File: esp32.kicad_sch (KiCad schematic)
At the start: 17 parts, among them Q3 BSS670S2, U2 ESP32-S3-WROOM-1U

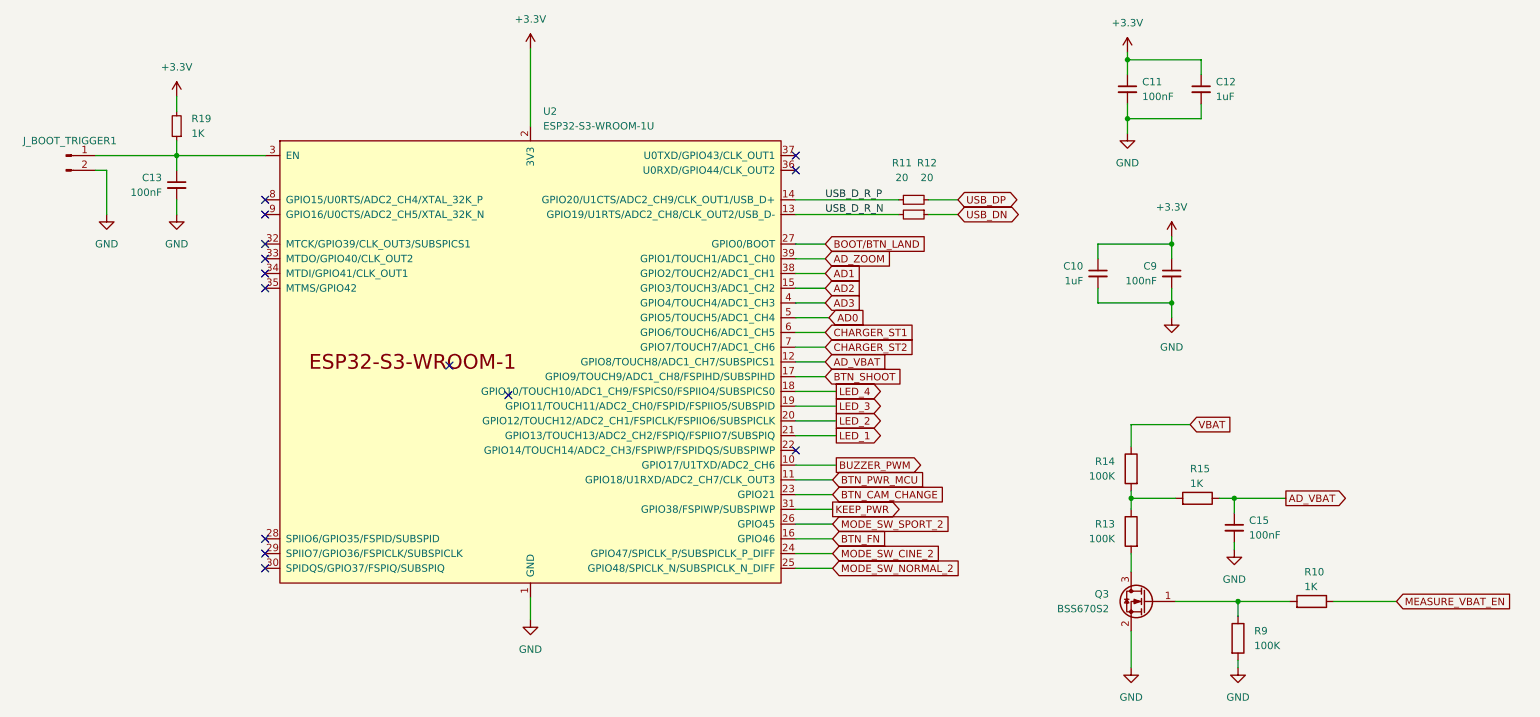
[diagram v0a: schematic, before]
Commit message: Board had been routedy
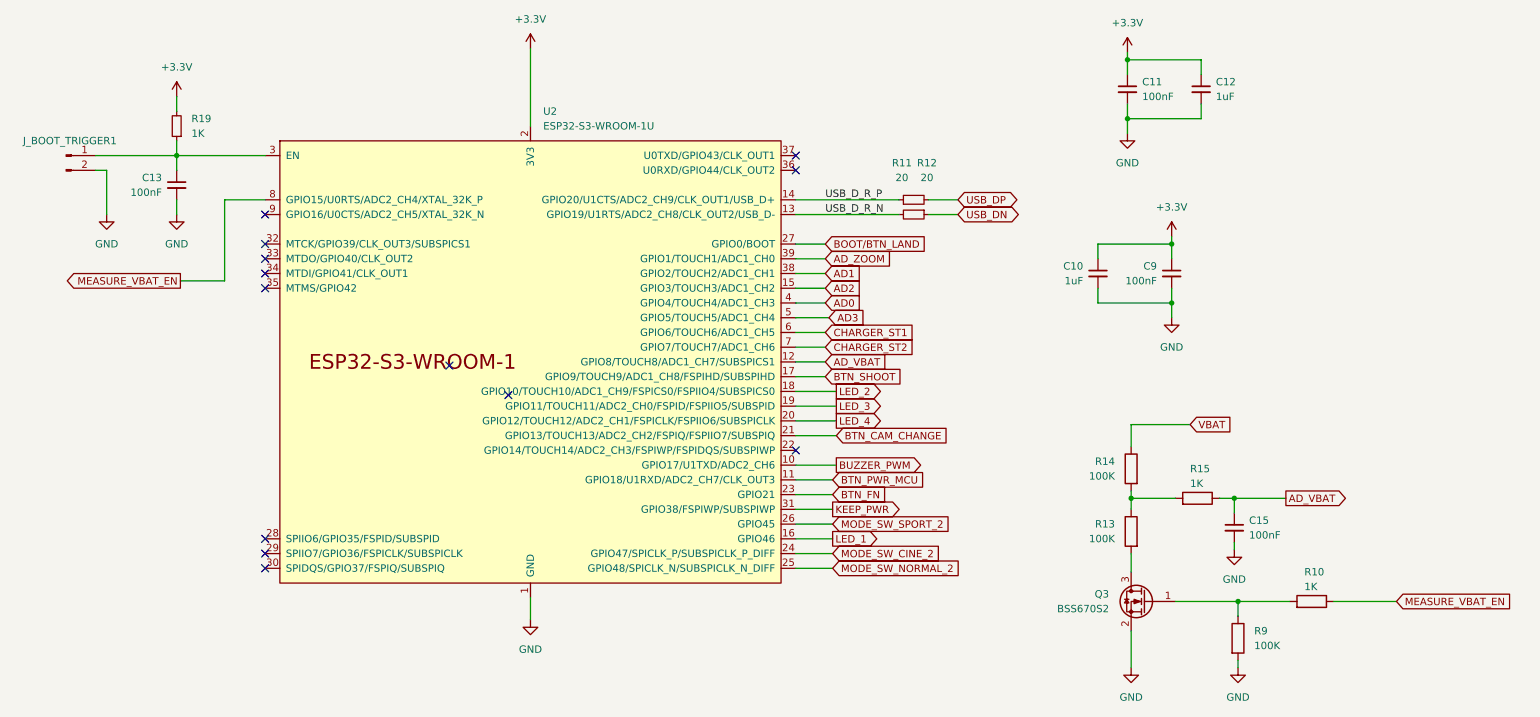
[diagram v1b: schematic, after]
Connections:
- net AD0: now also U2.4 (GPIO4/TOUCH4/ADC1_CH3); no longer U2.5 (GPIO5/TOUCH5/ADC1_CH4)
- net AD3: now also U2.5 (GPIO5/TOUCH5/ADC1_CH4); no longer U2.4 (GPIO4/TOUCH4/ADC1_CH3)
- net BTN_CAM_CHANGE: now also U2.21 (GPIO13/TOUCH13/ADC2_CH2/FSPIQ/FSPIIO7/SUBSPIQ); no longer U2.23 (GPIO21)
- net BTN_FN: now also U2.23 (GPIO21); no longer U2.16 (GPIO46)
- net LED_1: now also U2.16 (GPIO46); no longer U2.21 (GPIO13/TOUCH13/ADC2_CH2/FSPIQ/FSPIIO7/SUBSPIQ)
- net LED_2: now also U2.18 (GPIO10/TOUCH10/ADC1_CH9/FSPICS0/FSPIIO4/SUBSPICS0); no longer U2.20 (GPIO12/TOUCH12/ADC2_CH1/FSPICLK/FSPIIO6/SUBSPICLK)
- net LED_4: now also U2.20 (GPIO12/TOUCH12/ADC2_CH1/FSPICLK/FSPIIO6/SUBSPICLK); no longer U2.18 (GPIO10/TOUCH10/ADC1_CH9/FSPICS0/FSPIIO4/SUBSPICS0)
- net MEASURE_VBAT_EN: now also U2.8 (GPIO15/U0RTS/ADC2_CH4/XTAL_32K_P)
- no-connect marks 14 -> 13
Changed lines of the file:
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@@
-	)
-	(no_connect
-		(at 57.785 73.66)
 	)
 	(no_connect
@@
 	(wire
 		(pts
+			(xy 57.785 73.66) (xy 50.8 73.66)
+		)
+		(stroke
+			(width 0)
+			(type default)
+		)
+	)
+	(wire
+		(pts
 			(xy 103.505 142.24) (xy 103.505 146.05)
 		)
@@
 	(wire
 		(pts
+			(xy 50.8 73.66) (xy 50.8 87.63)
+		)
+		(stroke
+			(width 0)
+			(type default)
+		)
+	)
+	(wire
+		(pts
 			(xy 207.01 154.305) (xy 207.01 147.955)
 		)
@@
 		(pts
 			(xy 149.225 99.06) (xy 154.305 99.06)
+		)
+		(stroke
+			(width 0)
+			(type default)
+		)
+	)
+	(wire
+		(pts
+			(xy 50.8 87.63) (xy 43.18 87.63)
 		)
 		(stroke
@@
 			)
 			(justify left bottom)
+		)
+	)
+	(global_label "MEASURE_VBAT_EN"
+		(shape output)
+		(at 43.18 87.63 180)
+		(fields_autoplaced yes)
+		(effects
+			(font
+				(size 1.27 1.27)
+			)
+			(justify right)
+		)
+		(property "Intersheetrefs" "${INTERSHEET_REFS}"
+			(at 22.7173 87.63 0)
+			(hide yes)
+			(show_name no)
+			(do_not_autoplace no)
+			(effects
+				(font
+					(size 1.27 1.27)
+				)
+				(justify right)
+			)
 		)
 	)
@@
 		)
 	)
-	(global_label "AD3"
+	(global_label "AD0"
 		(shape input)
 		(at 154.305 91.44 0)
@@
 		)
 	)
-	(global_label "BTN_FN"
-		(shape input)
-		(at 155.575 132.08 0)
-		(fields_autoplaced yes)
-		(effects
-			(font
-				(size 1.27 1.27)
-			)
-			(justify left)
-		)
-		(property "Intersheetrefs" "${INTERSHEET_REFS}"
-			(at 165.515 132.08 0)
-			(hide yes)
-			(show_name no)
-			(do_not_autoplace no)
-			(effects
-				(font
-					(size 1.27 1.27)
-				)
-				(justify left)
-			)
-		)
-	)
-	(global_label "LED_1"
+	(global_label "LED_2"
 		(shape output)
-		(at 156.21 114.3 0)
-		(fields_autoplaced yes)
-		(effects
-			(font
-				(size 1.27 1.27)
-			)
-			(justify left)
-		)
-		(property "Intersheetrefs" "${INTERSHEET_REFS}"
-			(at 164.8194 114.3 0)
+		(at 156.21 106.68 0)
+		(fields_autoplaced yes)
+		(effects
+			(font
+				(size 1.27 1.27)
+			)
+			(justify left)
+		)
+		(property "Intersheetrefs" "${INTERSHEET_REFS}"
+			(at 164.8194 106.68 0)
 			(hide yes)
 			(show_name no)
@@
 		)
 	)
-	(global_label "BTN_CAM_CHANGE"
+	(global_label "BTN_FN"
 		(shape input)
 		(at 155.575 124.46 0)
@@
 		)
 		(property "Intersheetrefs" "${INTERSHEET_REFS}"
-			(at 175.3121 124.46 0)
+			(at 165.515 124.46 0)
 			(hide yes)
 			(show_name no)
@@
 		)
 	)
+	(global_label "BTN_CAM_CHANGE"
+		(shape input)
+		(at 156.21 114.3 0)
+		(fields_autoplaced yes)
+		(effects
+			(font
+				(size 1.27 1.27)
+			)
+			(justify left)
+		)
+		(property "Intersheetrefs" "${INTERSHEET_REFS}"
+			(at 175.9471 114.3 0)
+			(hide yes)
+			(show_name no)
+			(do_not_autoplace no)
+			(effects
+				(font
+					(size 1.27 1.27)
+				)
+				(justify left)
+			)
+		)
+	)
 	(global_label "MODE_SW_NORMAL_2"
 		(shape input)
@@
 		(property "Intersheetrefs" "${INTERSHEET_REFS}"
 			(at 178.0334 137.16 0)
-			(hide yes)
-			(show_name no)
-			(do_not_autoplace no)
-			(effects
-				(font
-					(size 1.27 1.27)
-				)
-				(justify left)
-			)
-		)
-	)
-	(global_label "AD_ZOOM"
-		(shape input)
-		(at 154.305 83.82 0)
-		(fields_autoplaced yes)
-		(effects
-			(font
-				(size 1.27 1.27)
-			)
-			(justify left)
-		)
-		(property "Intersheetrefs" "${INTERSHEET_REFS}"
-			(at 165.9383 83.82 0)
-			(hide yes)
-			(show_name no)
-			(do_not_autoplace no)
-			(effects
-				(font
-					(size 1.27 1.27)
-				)
-				(justify left)
-			)
-		)
-	)
-	(global_label "MODE_SW_CINE_2"
-		(shape input)
-		(at 155.575 134.62 0)
-		(fields_autoplaced yes)
-		(effects
-			(font
-				(size 1.27 1.27)
-			)
-			(justify left)
-		)
-		(property "Intersheetrefs" "${INTERSHEET_REFS}"
-			(at 174.8886 134.62 0)
-			(hide yes)
-			(show_name no)
-			(do_not_autoplace no)
-			(effects
-				(font
-					(size 1.27 1.27)
-				)
-				(justify left)
-			)
-		)
-	)
-	(global_label "BOOT{slash}BTN_LAND"
-		(shape input)
-		(at 154.305 81.28 0)
-		(fields_autoplaced yes)
-		(effects
-			(font
-				(size 1.27 1.27)
-			)
-			(justify left)
-		)
-		(property "Intersheetrefs" "${INTERSHEET_REFS}"
-			(at 172.7722 81.28 0)
 			(hide yes)
 			(show_name no)
@@
 	(global_label "LED_4"
 		(shape output)
-		(at 156.21 106.68 0)
-		(fields_autoplaced yes)
-		(effects
-			(font
-				(size 1.27 1.27)
-			)
-			(justify left)
-		)
-		(property "Intersheetrefs" "${INTERSHEET_REFS}"
-			(at 164.8194 106.68 0)
+		(at 156.21 111.76 0)
+		(fields_autoplaced yes)
+		(effects
+			(font
+				(size 1.27 1.27)
+			)
+			(justify left)
+		)
+		(property "Intersheetrefs" "${INTERSHEET_REFS}"
+			(at 164.8194 111.76 0)
+			(hide yes)
+			(show_name no)
+			(do_not_autoplace no)
+			(effects
+				(font
+					(size 1.27 1.27)
+				)
+				(justify left)
+			)
+		)
+	)
+	(global_label "AD_ZOOM"
+		(shape input)
+		(at 154.305 83.82 0)
+		(fields_autoplaced yes)
+		(effects
+			(font
+				(size 1.27 1.27)
+			)
+			(justify left)
+		)
+		(property "Intersheetrefs" "${INTERSHEET_REFS}"
+			(at 165.9383 83.82 0)
+			(hide yes)
+			(show_name no)
+			(do_not_autoplace no)
+			(effects
+				(font
+					(size 1.27 1.27)
+				)
+				(justify left)
+			)
+		)
+	)
+	(global_label "MODE_SW_CINE_2"
+		(shape input)
+		(at 155.575 134.62 0)
+		(fields_autoplaced yes)
+		(effects
+			(font
+				(size 1.27 1.27)
+			)
+			(justify left)
+		)
+		(property "Intersheetrefs" "${INTERSHEET_REFS}"
+			(at 174.8886 134.62 0)
+			(hide yes)
+			(show_name no)
+			(do_not_autoplace no)
+			(effects
+				(font
+					(size 1.27 1.27)
+				)
+				(justify left)
+			)
+		)
+	)
+	(global_label "BOOT{slash}BTN_LAND"
+		(shape input)
+		(at 154.305 81.28 0)
+		(fields_autoplaced yes)
+		(effects
+			(font
+				(size 1.27 1.27)
+			)
+			(justify left)
+		)
+		(property "Intersheetrefs" "${INTERSHEET_REFS}"
+			(at 172.7722 81.28 0)
 			(hide yes)
 			(show_name no)
@@
 		)
 	)
-	(global_label "LED_2"
+	(global_label "LED_1"
 		(shape output)
-		(at 156.21 111.76 0)
-		(fields_autoplaced yes)
-		(effects
-			(font
-				(size 1.27 1.27)
-			)
-			(justify left)
-		)
-		(property "Intersheetrefs" "${INTERSHEET_REFS}"
-			(at 164.8194 111.76 0)
+		(at 155.575 132.08 0)
+		(fields_autoplaced yes)
+		(effects
+			(font
+				(size 1.27 1.27)
+			)
+			(justify left)
+		)
+		(property "Intersheetrefs" "${INTERSHEET_REFS}"
+			(at 164.1844 132.08 0)
 			(hide yes)
 			(show_name no)
@@
 		)
 	)
-	(global_label "AD0"
+	(global_label "AD3"
 		(shape input)
 		(at 154.94 93.98 0)
